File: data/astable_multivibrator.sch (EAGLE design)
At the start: 8 parts, among them Q1 2N3904, Q2 2N3904

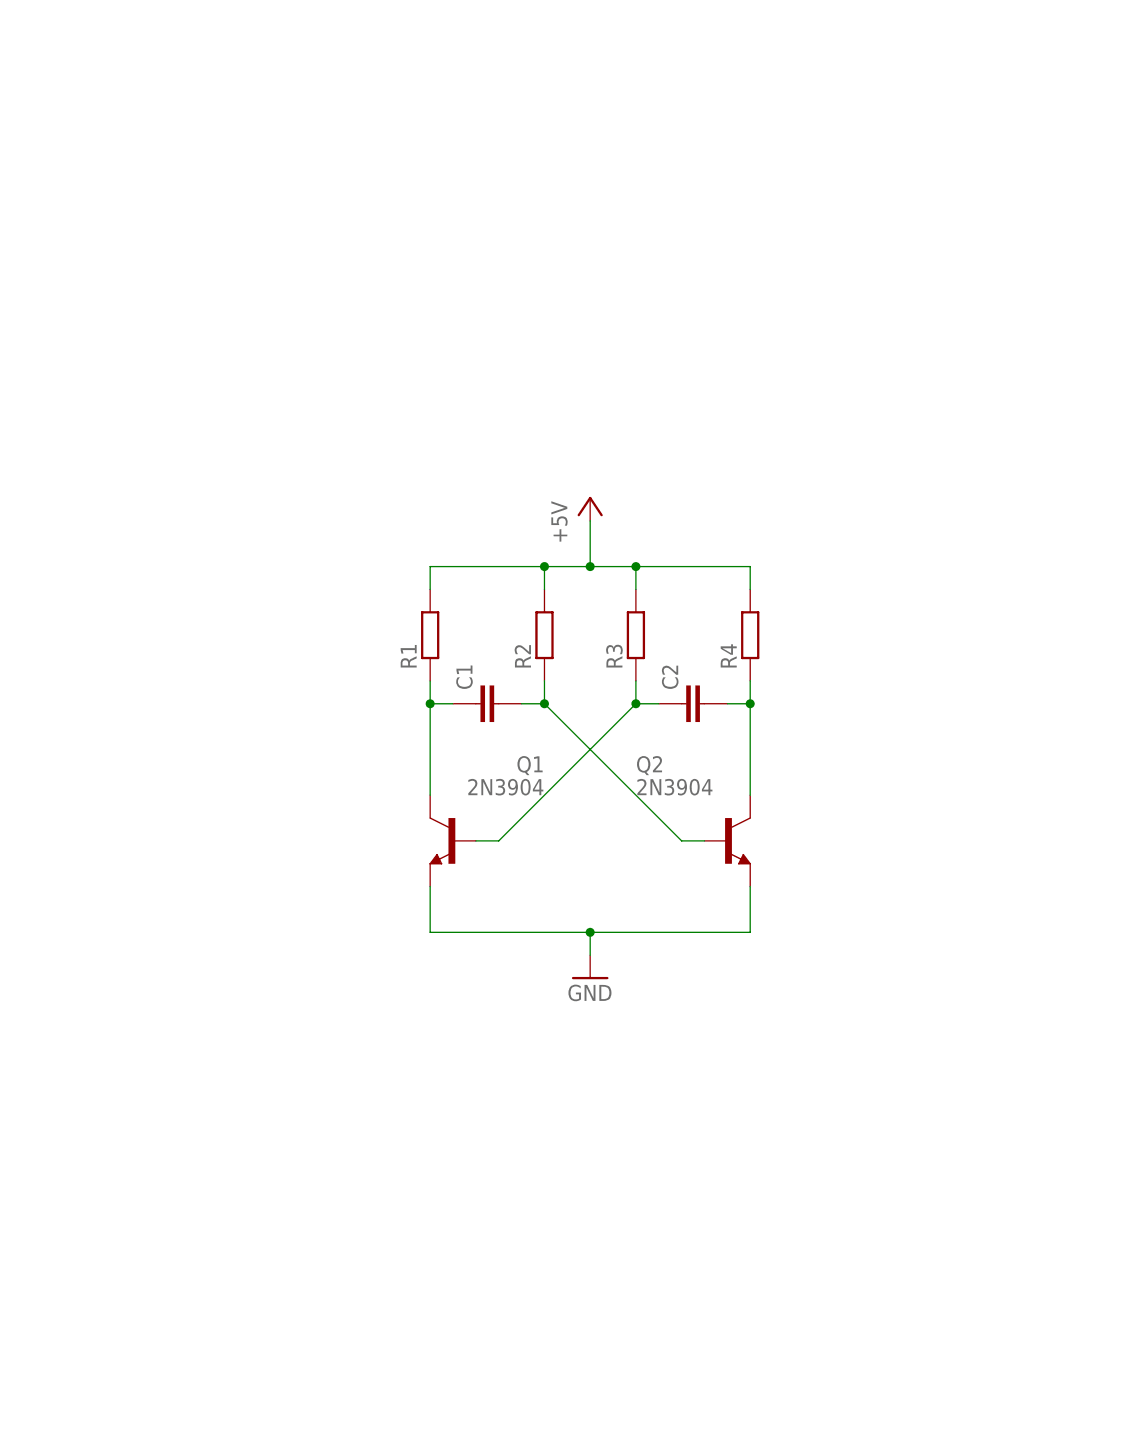
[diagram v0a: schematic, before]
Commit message: fix package information
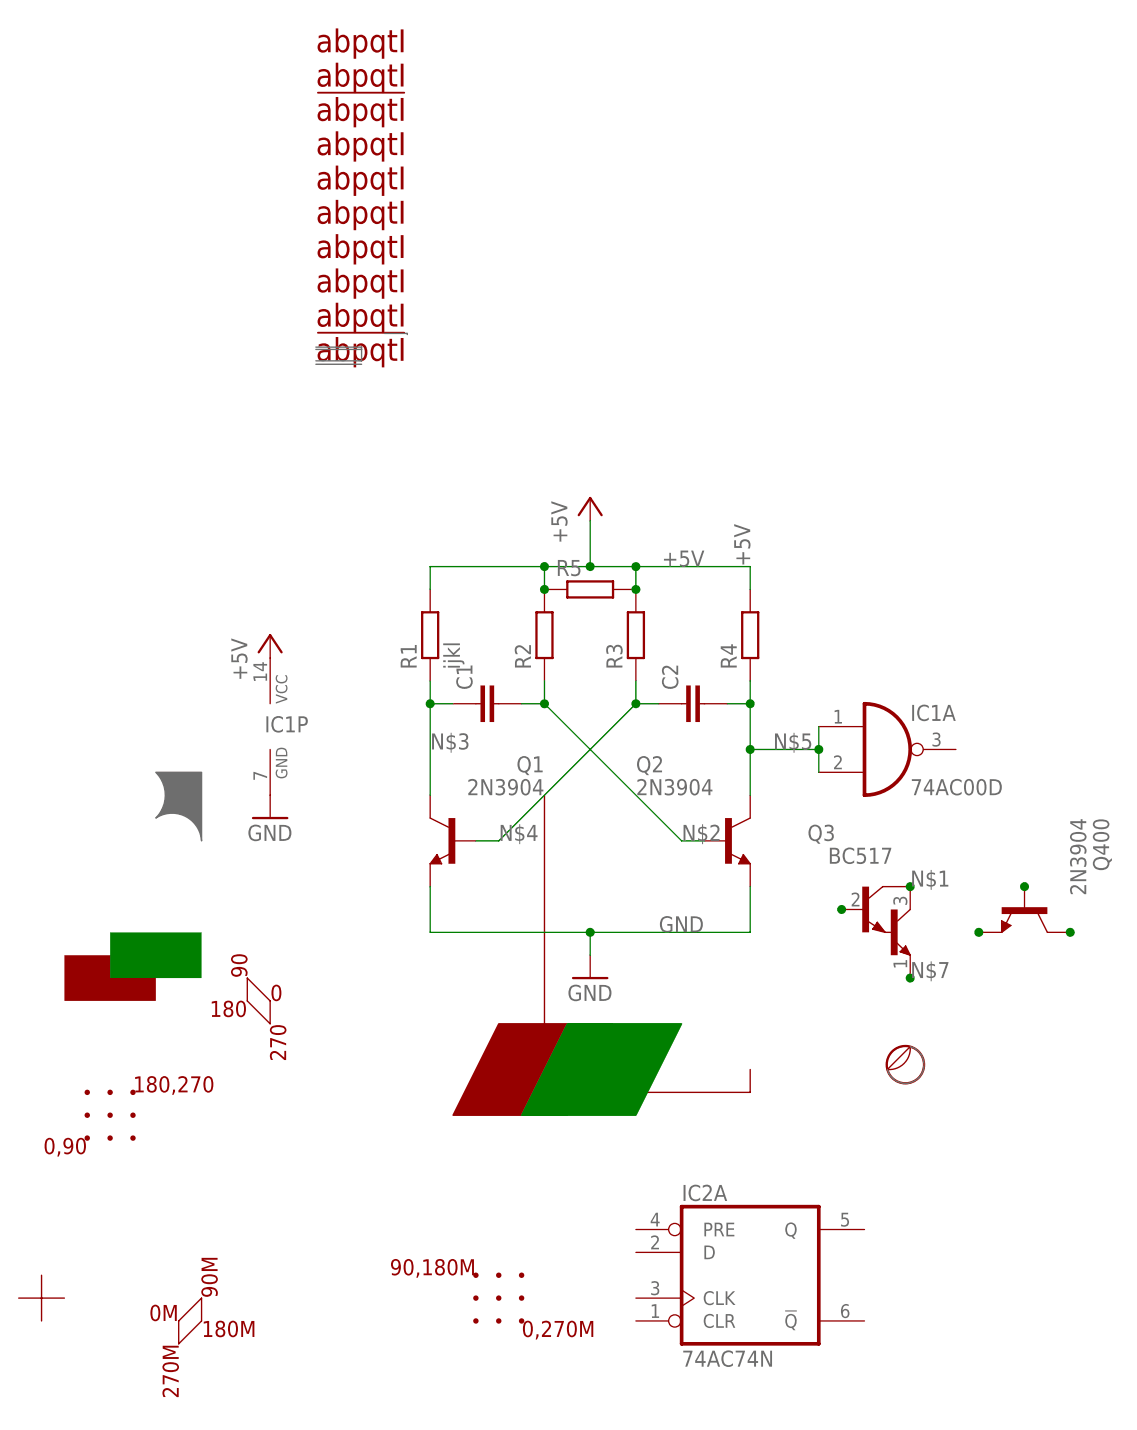
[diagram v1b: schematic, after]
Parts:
- added IC1: 74AC00D, 74xx-eu:74AC00D
- added IC2: 74AC74N, 74xx-eu:74AC74N
- added Q3: BC517, transistor-npn:BC517
- added Q400: 2N3904, transistor-npn:2N3904
- added R5: (no value), rcl:R-EU_M2012
- R1: value (none) -> ijkl; DIGIKEY (none) -> 114-5i4-1-ND
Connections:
- new net N$1: Q3.C
- new net N$10: Q400.C
- new net N$6: Q3.B
- new net N$7: Q3.E
- new net N$8: Q400.B
- new net N$9: Q400.E
- net +5V: now also IC1P.VCC, R5.1, R5.2
- net GND: now also IC1P.GND
- net N$5: now also IC1A.I0, IC1A.I1
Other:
- note added: "0"
- note added: "0,270M"
- note added: "0,90"
- note added: "0M"
- note added: "180"
- note added: "180,270"
- note added: "180M"
- note added: "270"
- note added: "270M"
- note added: "90"
- note added: "90,180M"
- note added: "90M"
- note added: "abpqtI abpqtI !abpqtI abpqtI abpqtI abpqtI abpqtI abpqtI abpqtI !abpqtI"
